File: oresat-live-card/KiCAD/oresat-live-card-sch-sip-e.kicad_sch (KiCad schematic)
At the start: 7 parts, among them J3 Conn_01x02, U7 OSD3358-512M-BSM

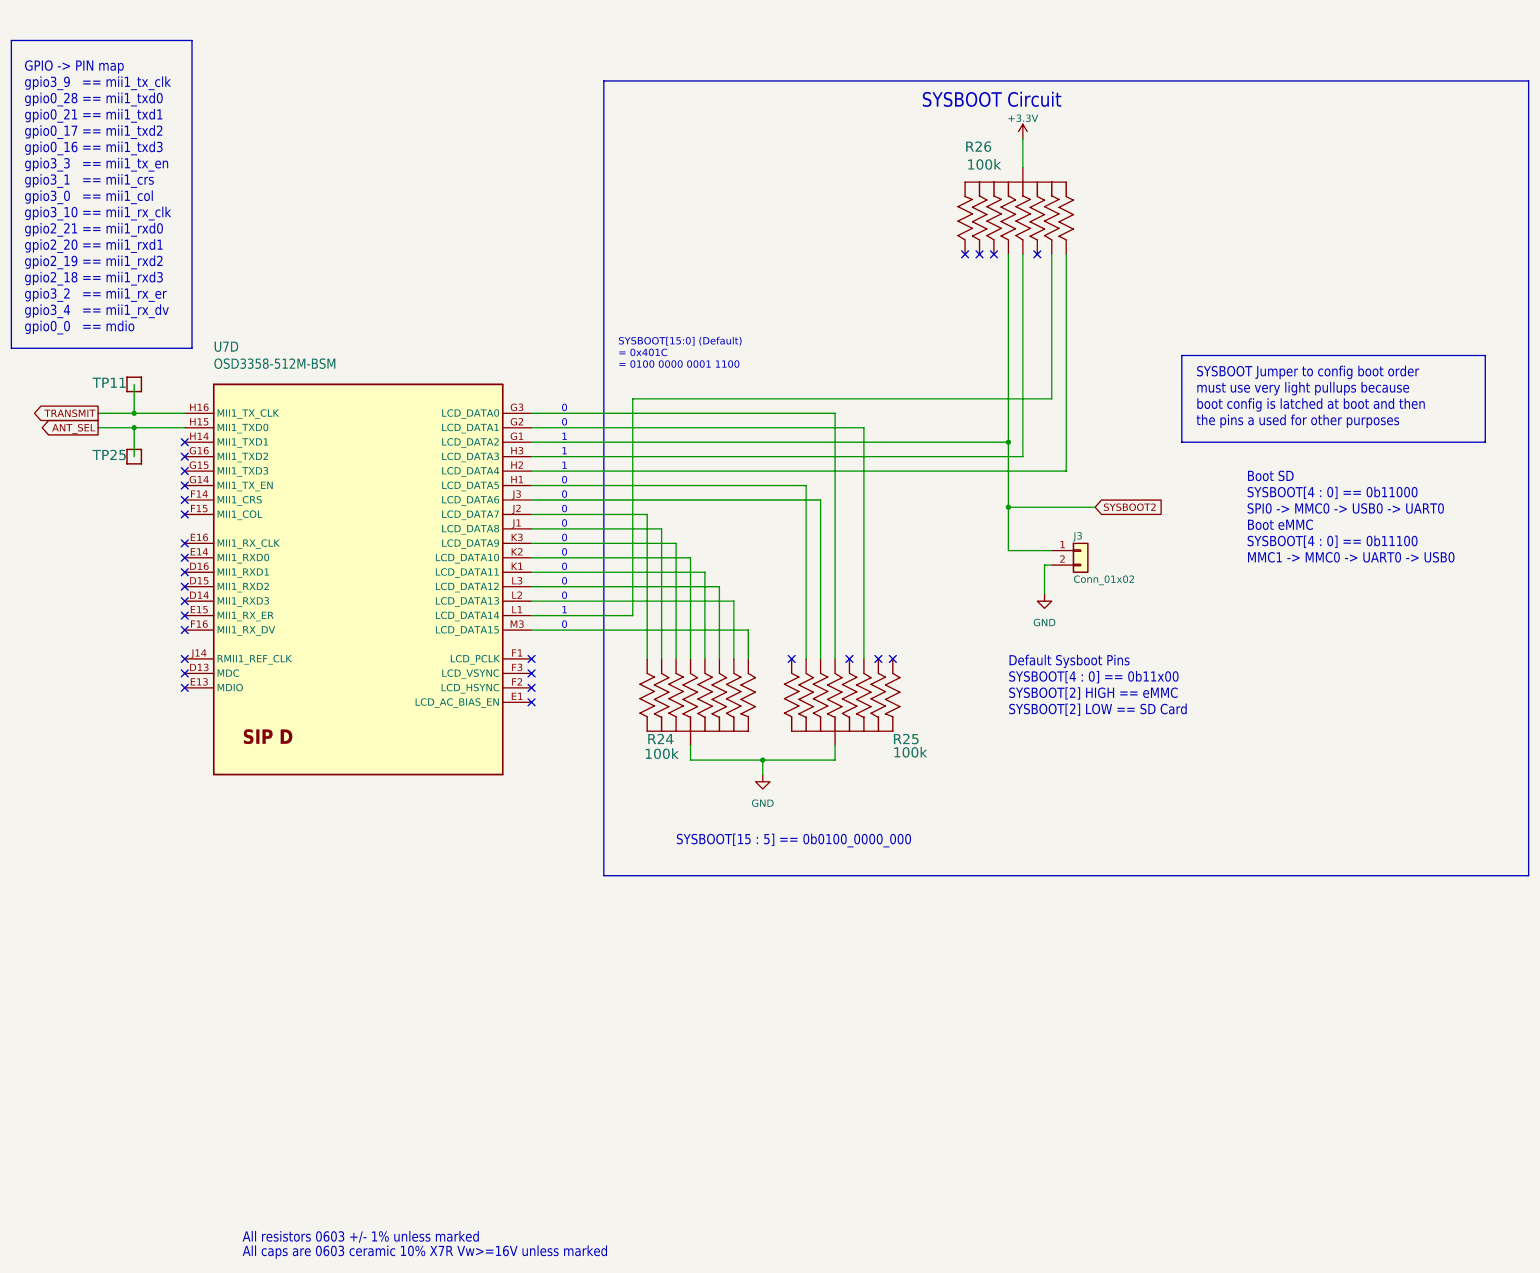
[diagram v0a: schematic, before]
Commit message: CLeaned up main connector, page names to be consistent with Octavo designs, sanity checks.
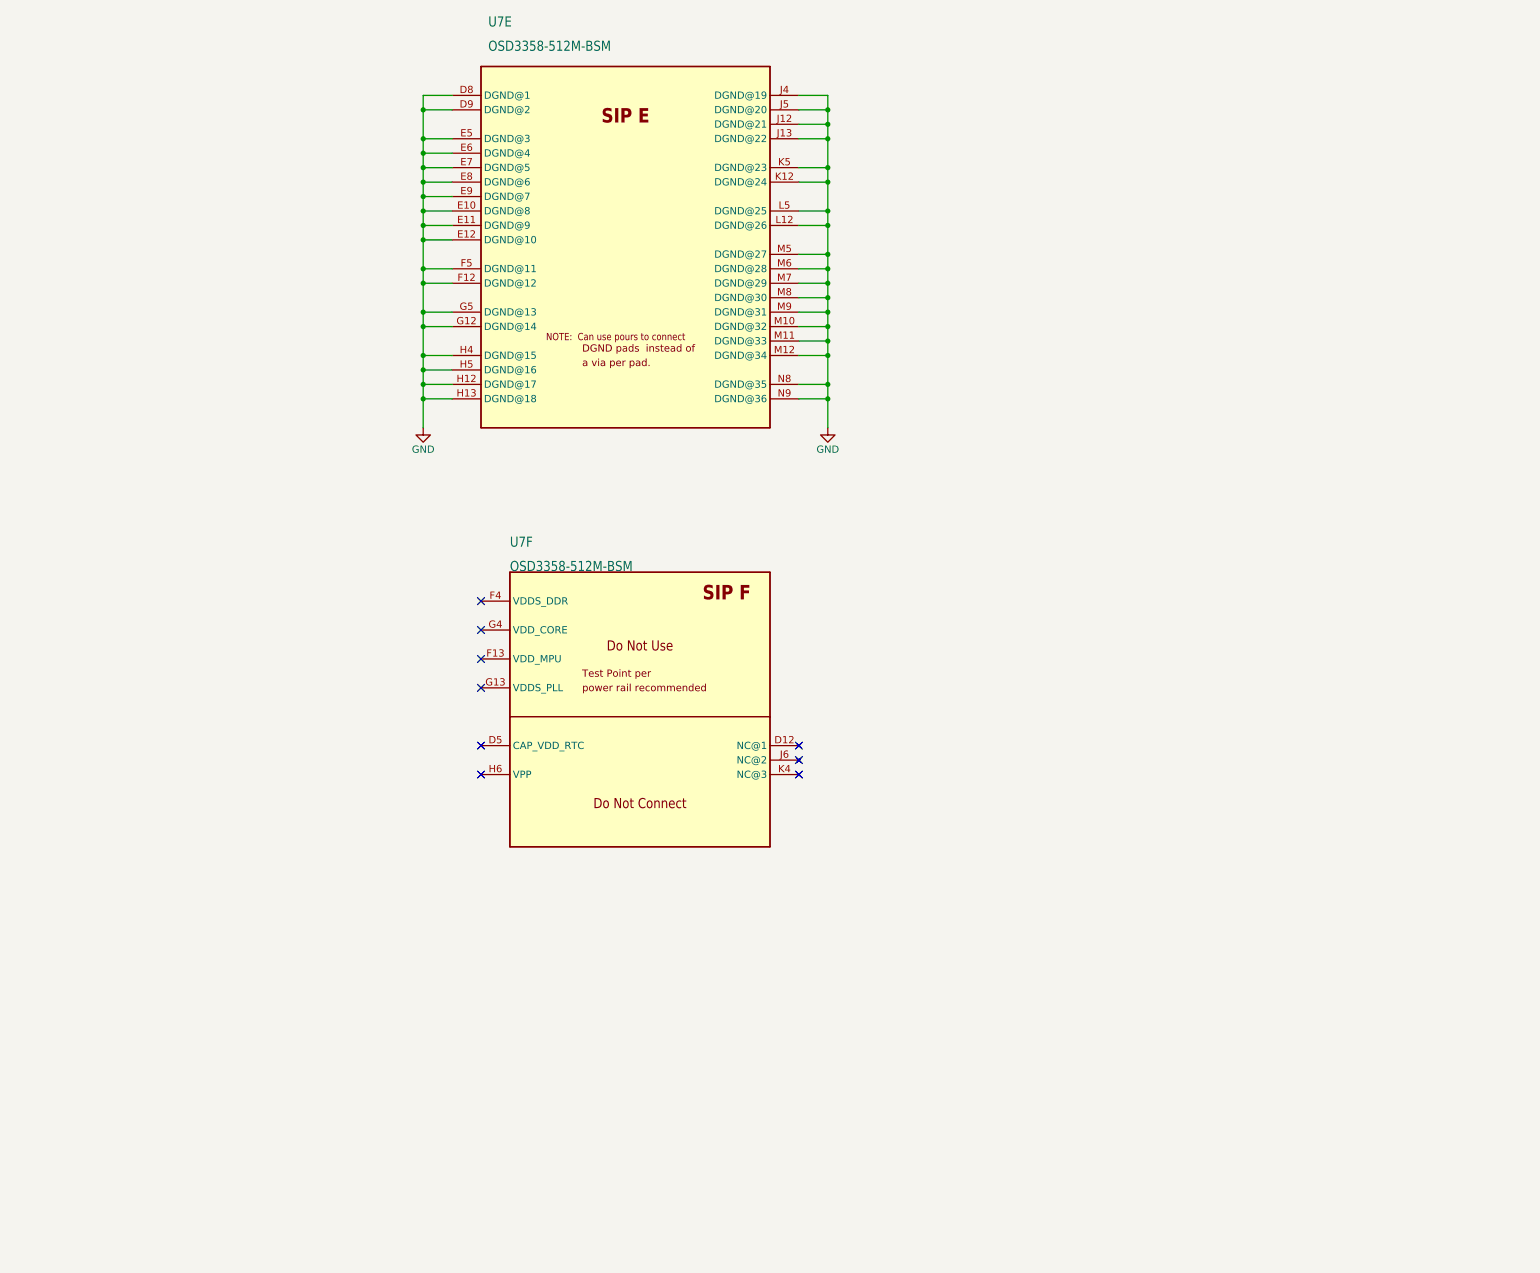
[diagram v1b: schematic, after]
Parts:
- removed J3: Conn_01x02, Connector_PinHeader_2.54mm:PinHeader_1x02_P2.54mm_Vertical, symbol Connector_Generic:Conn_01x02
- removed R24, R25, R26: 100k, oresat-live-card:ARRAY_EXBA-M, symbol oresat-passives:EXB-A10P391J
- removed TP11, TP25: TEST-POINT3X4, oresat-misc:TestPoint_Pad_D1.0mm, symbol oresat-misc:Test-Point-1mm-round
- removed U7: OSD3358-512M-BSM, oresat-ics:U-Octavo-OSD335X-BGA-256, symbol oresat-ics:OSD3358-512M-BSM
- added U7: OSD3358-512M-BSM, oresat-ics:U-Octavo-OSD335X-BGA-256, symbol oresat-ics:OSD3358-512M-BSM
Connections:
- net GND: now also U7.D8 (DGND@1), U7.D9 (DGND@2), U7.E10 (DGND@8), U7.E11 (DGND@9), U7.E12 (DGND@10), U7.E5 (DGND@3), U7.E6 (DGND@4), U7.E7 (DGND@5), U7.E8 (DGND@6), U7.E9 (DGND@7), U7.F12 (DGND@12), U7.F5 (DGND@11), U7.G12 (DGND@14), U7.G5 (DGND@13), U7.H12 (DGND@17), U7.H13 (DGND@18), U7.H4 (DGND@15), U7.H5 (DGND@16), U7.J12 (DGND@21), U7.J13 (DGND@22), U7.J4 (DGND@19), U7.J5 (DGND@20), U7.K12 (DGND@24), U7.K5 (DGND@23), U7.L12 (DGND@26), U7.L5 (DGND@25), U7.M10 (DGND@32), U7.M11 (DGND@33), U7.M12 (DGND@34), U7.M5 (DGND@27), U7.M6 (DGND@28), U7.M7 (DGND@29), U7.M8 (DGND@30), U7.M9 (DGND@31), U7.N8 (DGND@35), U7.N9 (DGND@36)
- no-connect marks 28 -> 9
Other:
- note removed: "0"
- note removed: "1"
- note removed: "All caps are 0603 ceramic 10% X7R Vw>=16V unless marked"
- note removed: "All resistors 0603 +/- 1% unless marked"
- note removed: "Boot SD SYSBOOT[4 : 0] == 0b11000 SPI0 -> MMC0 -> USB0 -> UART0 Boot eMMC SYSBOOT[4 : 0] == 0b11100 MMC1 -> MMC0 -> UART0 -> USB0"
- note removed: "Default Sysboot Pins SYSBOOT[4 : 0] == 0b11x00 SYSBOOT[2] HIGH == eMMC SYSBOOT[2] LOW == SD Card"
- note removed: "GPIO -> PIN map gpio3_9 == mii1_tx_clk gpio0_28 == mii1_txd0 gpio0_21 == mii1_txd1 gpio0_17 == mii1_txd2 gpio0_16 == mii1_txd3 gpio3_3 == mii1_tx_en gpio3_1 == mii1_crs gpio3_0 == mii1_col gpio3_10 == mii1_rx_clk gpio2_21 == mii1_rxd0 gpio2_20 == mii1_rxd1 gpio2_19 == mii1_rxd2 gpio2_18 == mii1_rxd3 gpio3_2 == mii1_rx_er gpio3_4 == mii1_rx_dv gpio0_0 == mdio"
- note removed: "SYSBOOT Circuit"
- note removed: "SYSBOOT Jumper to config boot order must use very light pullups because boot config is latched at boot and then the pins a used for other purposes"
- note removed: "SYSBOOT[15 : 5] == 0b0100_0000_000"
- note removed: "SYSBOOT[15:0] (Default) = 0x401C = 0100 0000 0001 1100"
